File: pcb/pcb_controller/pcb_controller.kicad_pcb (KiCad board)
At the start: 2 copper layers, 100 x 100 mm, 87 parts, among them IC300 OPA277, IC400 OPA277, IC401 OPA277, J100 JST_XH_B3B-XH, J101 JST_XH_B2B-XH, J102 XT30, J203 Banana conn, J300 Goldpin_2x3, J400 Conn_01x04, Q300 2N7002, Q301 2N7002, Q400 BC557, SW300 RotaryEncoder_Switch, U200 MC78L05, U201 MC79L05, U300 ATmega328P-A, U301 ADS1115IDGS, U302 REF3240, U303 MCP4725, U304 MCP4725, U500 TM1637, U501 CL5641BH, Y300 16MHz

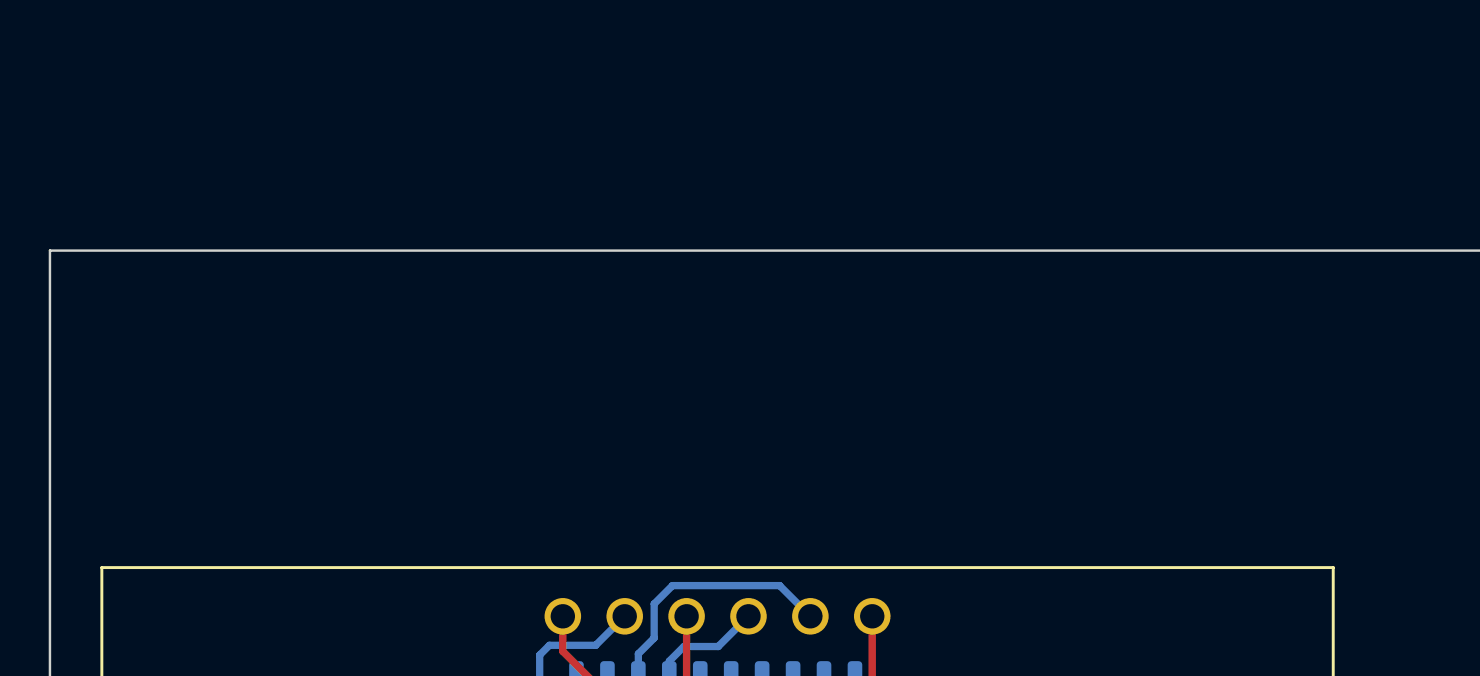
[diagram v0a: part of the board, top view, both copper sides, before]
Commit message: kicad 8.0
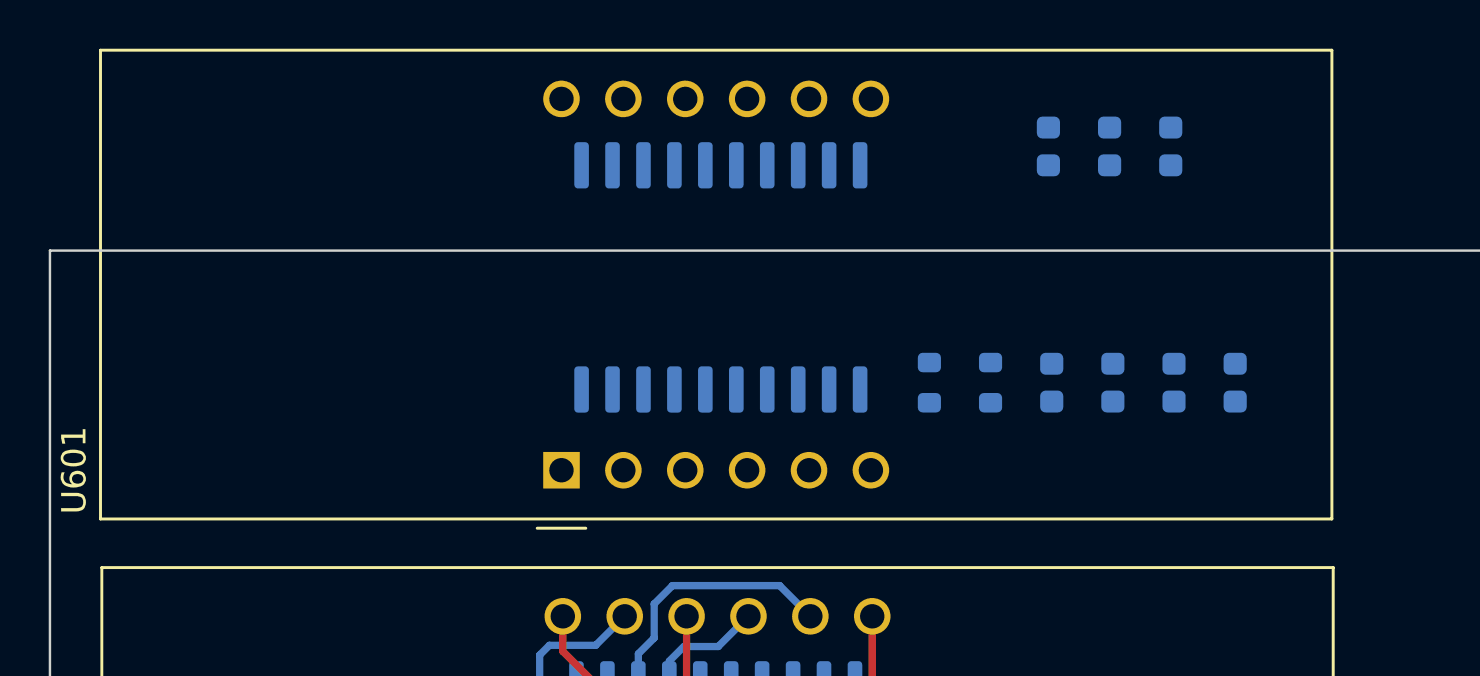
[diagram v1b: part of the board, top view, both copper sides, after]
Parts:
- added C500: 100p, Capacitor_SMD:C_0603_1608Metric, B.Cu at (46.0, -4.28)
- added C501: 100p, Capacitor_SMD:C_0603_1608Metric, B.Cu at (43.5, -4.28)
- added C503: 10u, Capacitor_SMD:C_0603_1608Metric, B.Cu at (41.0, -4.28)
- added C600: 100p, Capacitor_SMD:C_0603_1608Metric, B.Cu at (48.6, 5.42)
- added C601: 100p, Capacitor_SMD:C_0603_1608Metric, B.Cu at (46.1, 5.42)
- added C602: 100n, Capacitor_SMD:C_0603_1608Metric, B.Cu at (43.6, 5.42)
- added C603: 10u, Capacitor_SMD:C_0603_1608Metric, B.Cu at (41.1, 5.42)
- added R600: 10k, Resistor_SMD:R_0603_1608Metric, B.Cu at (38.6, 5.42)
- added R601: 10k, Resistor_SMD:R_0603_1608Metric, B.Cu at (36.1, 5.42)
- added U600: TM1637, Package_SO:SOP-20_7.5x12.8mm_P1.27mm, B.Cu at (27.5, 1.10)
- added U601: CL5641BH, Display_7Segment:CA56-12SURKWA, F.Cu at (21.0, 9.02)
- R500, R501: value 4k7 -> 10k
- renumbered C500 to C502
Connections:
- net Net-(R308-Pad2) renamed /MCU/_e_B
- net Net-(R309-Pad2) renamed /MCU/_e_A
- net Net-(R312-Pad1) renamed /MCU/_e_bt
- C502 pad 1: GND -> +5V
- C502 pad 2: +5V -> GND
- R500 pad 2: /MCU/4 digit LED display V/DIO -> /MCU/U_disp_DIO
- R501 pad 2: /MCU/4 digit LED display V/CLK -> /MCU/U_disp_CLK
- U300 pad 10: unconnected-(U300-PD6-Pad10) -> /MCU/U_disp_DIO
- U300 pad 11: unconnected-(U300-PD7-Pad11) -> /MCU/U_disp_CLK
- U300 pad 2: unconnected-(U300-PD4-Pad2) -> /MCU/I_disp_DIO
- U300 pad 9: unconnected-(U300-PD5-Pad9) -> /MCU/I_disp_CLK
- U500 pad 17: /MCU/4 digit LED display V/DIO -> /MCU/U_disp_DIO
- U500 pad 18: /MCU/4 digit LED display V/CLK -> /MCU/U_disp_CLK

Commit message: most analog layout
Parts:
- added C604: 10u, Capacitor_THT:CP_Radial_D5.0mm_P2.00mm, B.Cu at (61.6, 91.5)
- added J301: JST_XH_B3B-XH, Connector_JST:JST_XH_B3B-XH-A_1x03_P2.50mm_Vertical, F.Cu at (113.5, 37.9)
- added Q302: CJ2306, Package_TO_SOT_SMD:SOT-23, F.Cu at (107.6, 36.9)
- added Q303: 2N7002, Package_TO_SOT_SMD:SOT-23, F.Cu at (107.6, 41.6)
- added Q304: BSS83P, Package_TO_SOT_SMD:SOT-23, F.Cu at (107.6, 46.2)
- added Q305: CJ2306, Package_TO_SOT_SMD:SOT-23, F.Cu at (119.0, 49.7)
- added R314: 220R, Resistor_SMD:R_0603_1608Metric, F.Cu at (103.1, 35.8)
- added R315: 220R, Resistor_SMD:R_0603_1608Metric, F.Cu at (103.1, 38.3)
- added R316: 10k, Resistor_SMD:R_0603_1608Metric, F.Cu at (103.1, 40.8)
- added R317: 10k, Resistor_SMD:R_0603_1608Metric, F.Cu at (103.1, 43.3)
- added R318: 10k, Resistor_SMD:R_0603_1608Metric, F.Cu at (103.1, 45.8)
- added R319: 220R, Resistor_SMD:R_0603_1608Metric, F.Cu at (103.1, 48.4)
- added R320: 10k, Resistor_SMD:R_0603_1608Metric, F.Cu at (103.1, 50.9)
- added R321: 10k, Resistor_SMD:R_0603_1608Metric, F.Cu at (103.1, 53.4)
- C403, Q300, Q301, R402, R404, R406, R407: moved to B.Cu
- J400: value Conn_01x04 -> JST_XH_B4B-XH
- Q400: value BC557 -> S9015
- R308: renamed from R306; moved to B.Cu
- R309: renamed from R307; moved to B.Cu
- R310: renamed from R300; moved to B.Cu
- R322: renamed from R314; moved to B.Cu
- R323: renamed from R315; moved to B.Cu
- U301: renamed from U302; moved to B.Cu
- U302: renamed from U303; moved to B.Cu
- U303: renamed from U304; moved to B.Cu
- U304: renamed from U301; moved to B.Cu
- moved J100 98.7 mm to (94.7, 48.8), turned to 180 degrees
- moved D202 85.6 mm to (97.5, 60.7), turned to -90 degrees
- moved D203 83.7 mm to (93.9, 60.7), turned to -90 degrees
- moved D200 76.3 mm to (90.3, 60.6), turned to 90 degrees
- moved D201 74.3 mm to (86.7, 60.6), turned to 90 degrees
- moved C200 66.7 mm to (93.7, 68.2)
- moved C201 66.7 mm to (93.7, 77.1)
- moved U303 61.4 mm to (34.6, 71.5), turned to 180 degrees
- moved C307 59.1 mm to (32.6, 91.2), turned to 180 degrees
- moved U302 59.0 mm to (34.6, 75.6), turned to 180 degrees
- moved IC300 57.5 mm to (33.7, 91.8), turned to -90 degrees
- moved U301 57.2 mm to (34.6, 79.7), turned to 180 degrees
- moved C308 56.2 mm to (34.8, 93.7), turned to 180 degrees
- moved R308 55.8 mm to (29.6, 75.6), turned to -90 degrees
- moved R313 55.3 mm to (33.7, 95.1), turned to 180 degrees
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- renumbered C307 to C300, C308 to C301, C300 to C302, C301 to C303, C310 to C304, C302 to C307, C303 to C308, C304 to C310, R308 to R300, R309 to R301, R310 to R302, R311 to R303, R312 to R304, R313 to R305, R304 to R306, R305 to R307, R301 to R311, R302 to R312, R303 to R313
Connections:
- C408 pad 1: -5V -> GND
- C408 pad 2: GND -> -5V
- C409 pad 1: GND -> +5V
- C409 pad 2: +5V -> GND
- C410 pad 1: -5V -> GND
- C410 pad 2: GND -> -5V
- J400 pad 1: unconnected-(J400-Pin_1-Pad1) -> /MCU/relay1
- J400 pad 2: unconnected-(J400-Pin_2-Pad2) -> /MCU/relay2
- J400 pad 3: unconnected-(J400-Pin_3-Pad3) -> +12V
- R310 pad 1: /MCU/+Vout_sense -> GND
- R311 pad 1: /MCU/-Vout_sense -> /Linear regulator/-Vin
- R322 pad 2: /MCU/I_set -> /Linear regulator/I_set
- R323 pad 1: /MCU/I_set -> /Linear regulator/I_set
- U302 pad 1: /MCU/U_set -> /Linear regulator/U_set
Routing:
- net GND: track 12.9 -> 131.4 mm, vias 0 -> 11
- net /Linear regulator/-Vin: track 12.8 -> 49.2 mm, vias 0 -> 1
- net I_meas: track 8.08 -> 38.5 mm, vias 0 -> 2
- net +5V: track 0.00 -> 29.9 mm, vias 0 -> 4
- net /Power/-9V_unreg: track 0.00 -> 26.9 mm
- net +4V: track 0.00 -> 24.9 mm, vias 0 -> 5
- net /Power/-7VAC: track 0.00 -> 23.4 mm, vias 0 -> 3
- net /Power/+7VAC: track 0.00 -> 19.6 mm
- net /Linear regulator/I_set: track 0.00 -> 19.3 mm, vias 0 -> 2
- net /Power/+9V_unreg: track 0.00 -> 12.6 mm
- net /Linear regulator/Vout_div: track 0.00 -> 11.8 mm
- net /MCU/Vout_meas: track 0.00 -> 11.2 mm
- net /MCU/SDA_4V: track 0.00 -> 7.18 mm
- net /Linear regulator/+in_CV_amp: track 0.00 -> 6.17 mm, vias 0 -> 1
- net /MCU/SCL_4V: track 0.00 -> 5.99 mm, vias 0 -> 2
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- added copper zone on B.Cu, net /Linear regulator/-Vin
- added copper zone on B.Cu, net GND
- added copper zone on B.Cu, net I_meas

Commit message: minor changes
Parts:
- C300, C301, C304, C400, J301, Q302, Q303, Q304, Q305, Q400, R300, R301, R302, R303, R304, R305, R314, R315, R316, R317, R318, R319, R320, R321, R400, RV400: moved to B.Cu
- moved Q304 100.1 mm to (9.20, 64.5), turned to 90 degrees
- moved Q303 97.3 mm to (13.1, 64.5), turned to 90 degrees
- moved R318 96.5 mm to (9.10, 67.5)
- moved R317 93.1 mm to (13.2, 67.5), turned to 180 degrees
- moved Q305 91.0 mm to (28.0, 52.8), turned to 90 degrees
- moved R315 90.8 mm to (16.9, 66.8), turned to -90 degrees
- moved Q302 87.1 mm to (21.9, 52.7), turned to 90 degrees
- moved R320 86.8 mm to (17.1, 62.6), turned to -90 degrees
- moved R316 82.6 mm to (21.9, 55.8), turned to 180 degrees
- moved R314 80.6 mm to (24.8, 55.0), turned to -90 degrees
- moved R321 75.1 mm to (28.1, 55.8), turned to 180 degrees
- moved R319 72.6 mm to (30.7, 53.3), turned to -90 degrees
- moved J300 58.8 mm to (4.25, 87.2), turned to 0 degrees
- moved C303 48.2 mm to (23.3, 93.5), turned to -90 degrees
- moved J301 41.4 mm to (73.6, 49.1), turned to 180 degrees
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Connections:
- R320 pad 1: +12V -> +5V
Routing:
- net Net-(U600-SEG1/KS1): track 0.00 -> 22.4 mm
- net Net-(U600-GRID4): track 0.00 -> 19.3 mm, vias 0 -> 1
- net +5V: track 29.9 -> 44.2 mm
- net Net-(U600-SEG5/KS5): track 0.00 -> 13.8 mm
- net Net-(U600-SEG2/KS2): track 0.00 -> 13.3 mm, vias 0 -> 1
- net Net-(U600-SEG6/KS6): track 0.00 -> 12.3 mm, vias 0 -> 1
- net /MCU/MISO: track 0.00 -> 11.3 mm, vias 0 -> 1
- net Net-(U600-SEG7/KS7): track 0.00 -> 11.1 mm, vias 0 -> 1
- net Net-(U600-GRID3): track 0.00 -> 10.9 mm
- net Net-(U600-GRID1): track 0.00 -> 9.69 mm, vias 0 -> 1
- net /MCU/SCK: track 0.00 -> 9.10 mm
- net Net-(U600-SEG8/KS8): track 0.00 -> 8.82 mm
- net /MCU/MOSI: track 0.00 -> 7.53 mm
- net Net-(U600-SEG4/KS4): track 0.00 -> 6.93 mm
- net /MCU/XTAL2: track 0.00 -> 6.36 mm, vias 0 -> 1
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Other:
- outline, holes or cut-outs redrawn
